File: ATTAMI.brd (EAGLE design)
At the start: 22.8 x 22.9 mm, 19 parts, among them J1 CON_HEADER_1X02-PTH, J2 MICRO-USB_ALIEXPRESS, J3 CON_HEADER_1X02-PTH, J4 CON_HEADER_1X06-PTH, U1 MIC5225, U2 ATTINY85

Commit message: ver 15b05
now the polygon back silkscreen logo placed correctly, ready for panalizing(!)
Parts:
- moved D4 0.37 mm to (20.5, 16.5)

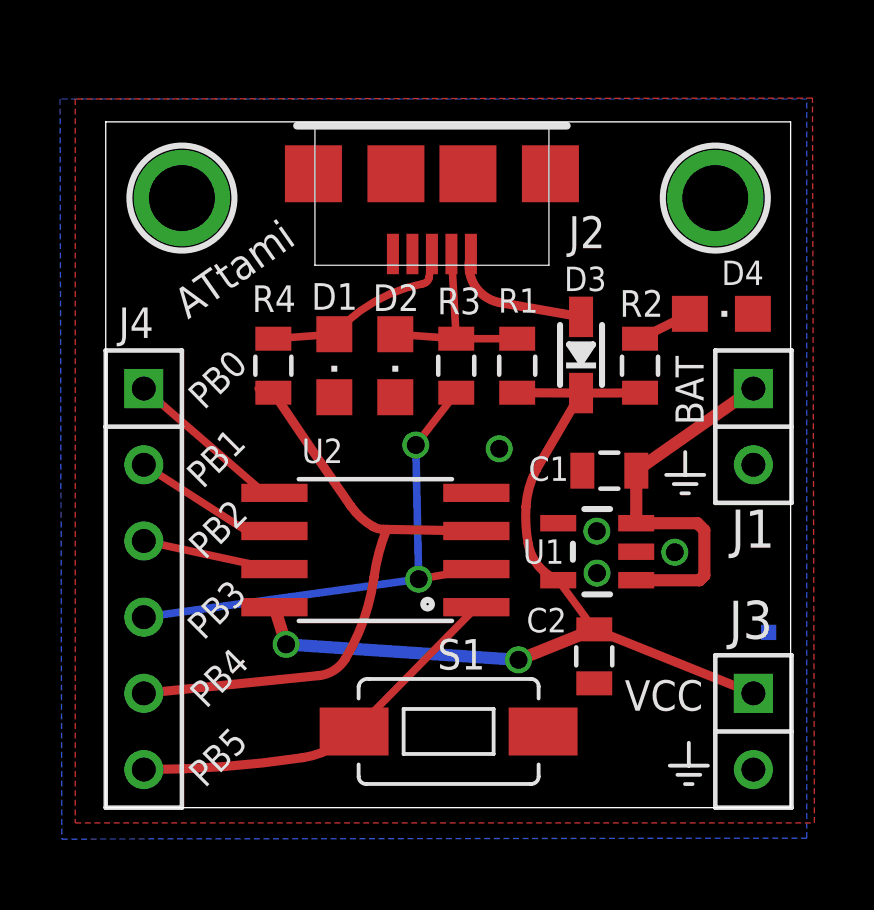
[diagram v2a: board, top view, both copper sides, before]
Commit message: 15b06
because of sobbing of online gerber checker 
https://www.freedfm.com/freedfm/0022376203858107/results/summary2.htm
- enlarge fonts on silkscreen to min 5mil 
- removed some redundant polygons from bottom silk
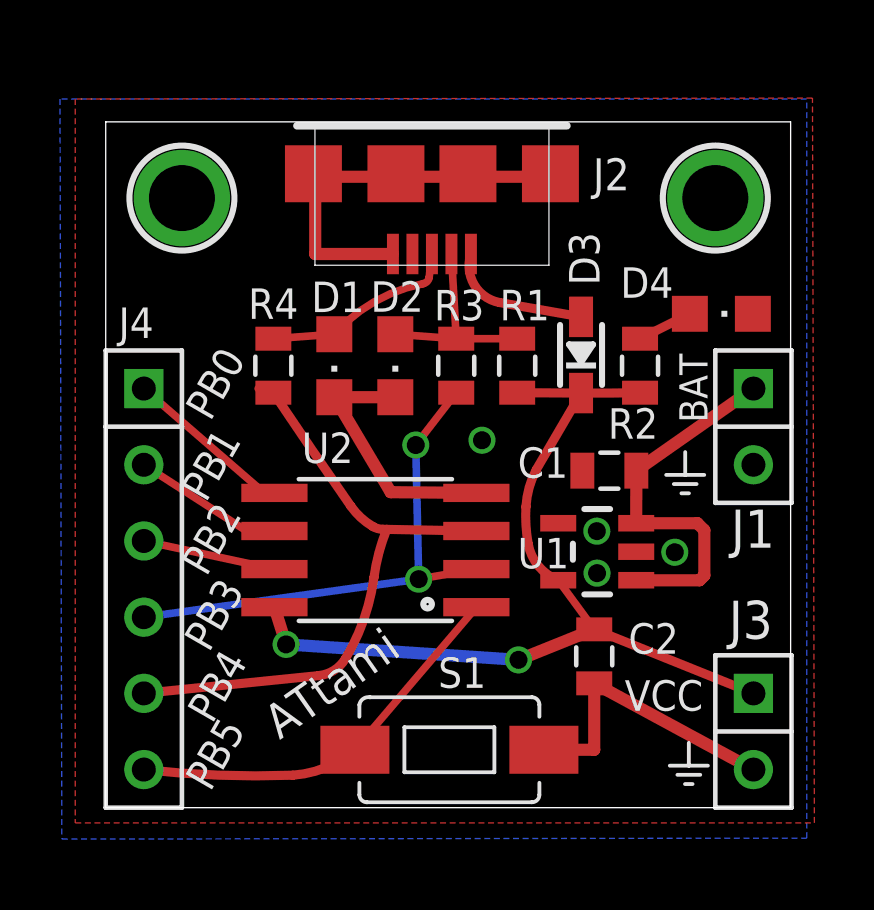
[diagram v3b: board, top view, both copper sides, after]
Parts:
- moved S1 0.61 mm to (11.5, 1.93)
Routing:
- net GND: track 0.00 -> 31.6 mm

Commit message: ver 17
changed the USB connector to the "official" package
MOLEX - 47346-0001 - MICRO USB TYPE B
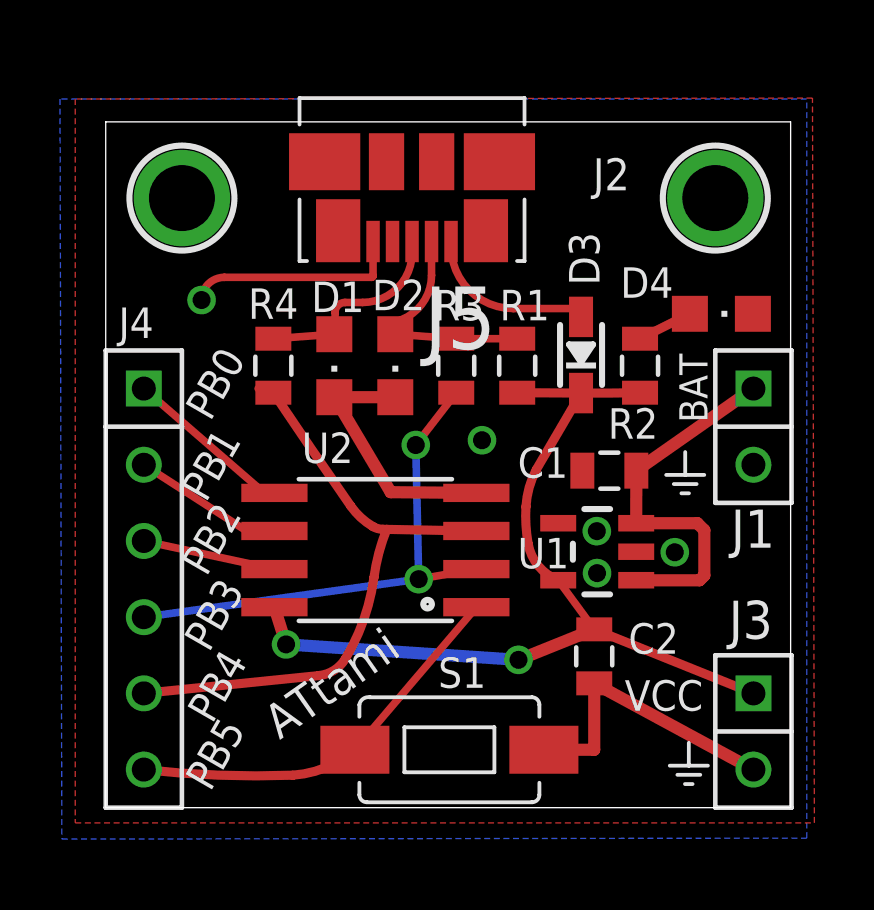
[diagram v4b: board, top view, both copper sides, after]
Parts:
- removed J2: MICRO-USB_ALIEXPRESS, yair_r:USB-MICRO-ALIEXPRESS
- added J5: (no value), Molex-47346-0001:MOLEX_47346-0001
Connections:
- removed net N$10: D2.A, J2.DM, R1.2, R3.1
- removed net N$7: D1.A, J2.DP, R4.1
- new net DM: D2.A, J5.2, R1.2, R3.1
- new net DP: D1.A, J5.3, R4.1
- net GND: now also J5.5; no longer J2.GND@1, J2.GND@2, J2.GND@3
- net V-BUS: now also J5.1; no longer J2.VCC
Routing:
- net DM: track 0.00 -> 7.98 mm
- net N$10: track 6.90 -> 0.00 mm
- net DP: track 0.00 -> 6.54 mm
- net N$7: track 6.52 -> 0.00 mm
- net GND: track 31.6 -> 25.7 mm, vias 4 -> 5
- net V-BUS: track 4.64 -> 5.47 mm

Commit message: sent to FAB
geekcon edition, with coincell
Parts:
- removed J4: CON_HEADER_1X06-PTH, dp_devices:M1X6
- removed J5: (no value), Molex-47346-0001:MOLEX_47346-0001
- added COIN_CELL, COIN_CELL_GND: (no value), adafruit:1X01-CLEANBIG
- added D5: Schottky, microbuilder:SOD-323
- added J2: (no value), microbuilder:1X02_ROUND
- added SJ1: (no value), microbuilder:SOLDERJUMPER_CLOSEDWIRE
- added USB: MICRO-USB_ALIEXPRESS, yair_r:USB-MICRO-ALIEXPRESS
- J1: value CON_HEADER_1X02-PTH -> (none); device dp_devices:M1X2 -> microbuilder:1X07_ROUND
- J3: value CON_HEADER_1X02-PTH -> (none); device dp_devices:M1X2 -> microbuilder:1X02_ROUND
- R2: value 560R -> 1K5
- moved J1 20.7 mm to (1.27, 8.89)
- moved C2 9.84 mm to (6.45, 5.37), turned to 0 degrees
- moved R2 1.22 mm to (18.2, 13.6)
- moved U2 0.65 mm to (8.85, 9.22)
- moved D3 0.42 mm to (16.1, 15.4)
- moved S1 0.28 mm to (11.2, 1.80)
- moved D4 0.25 mm to (20.8, 16.5), turned to 90 degrees
- moved D2 0.15 mm to (9.65, 14.6)
- moved D1 0.13 mm to (7.65, 14.6)
- moved C1 0.12 mm to (16.8, 11.1)
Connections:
- removed net DM: D2.A, J5.2, R1.2, R3.1
- removed net DP: D1.A, J5.3, R4.1
- new net N$10: D2.A, R1.2, R3.1, USB.DM
- new net N$13: D4.C, SJ1.2
- new net N$4: COIN_CELL.1, D5.AQ
- new net N$7: D1.A, R4.1, USB.DP
- net GND: now also COIN_CELL_GND.1, J1.1, J2.2, SJ1.1, USB.GND@1, USB.GND@2, USB.GND@3, USB.P$10, USB.P$9; no longer D4.C, J1.2, J5.5
- net N$1: now also J1.5; no longer J4.4
- net N$15: now also J1.3; no longer J4.2
- net N$3: now also J1.2; no longer J4.1
- net N$5: now also J1.4; no longer J4.3
- net N$6: now also J1.6; no longer J4.5
- net N$8: now also J1.7; no longer J4.6
- net V-BUS: now also D3.AQ, USB.VCC; no longer D3.A, J5.1
- net VCC: now also D3.CQ, D5.CQ; no longer D3.C
- net V_BAT: now also J2.1; no longer J1.1
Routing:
- net GND: track 25.7 -> 8.52 mm, vias 5 -> 4
- net DM: track 7.98 -> 0.00 mm
- net N$10: track 0.00 -> 6.97 mm
- net VCC: track 30.7 -> 37.5 mm
- net N$7: track 0.00 -> 6.72 mm
- net DP: track 6.54 -> 0.00 mm
- net V_BAT: track 12.8 -> 6.82 mm
- net N$13: track 0.00 -> 3.34 mm, vias 0 -> 1
- net N$4: track 0.00 -> 2.77 mm
- net N$11: track 1.86 -> 4.18 mm
- net N$6: track 21.0 -> 22.8 mm
- net N$8: track 13.4 -> 15.0 mm
- net N$1: track 17.9 -> 16.7 mm

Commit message: fix floating pin
major error in voltage regualtor (U1).  enable pin was not connected to
VBAT in GKx  batch :(.
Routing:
- net V_BAT: track 6.82 -> 11.2 mm
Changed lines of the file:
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@@
 <wire x1="17.69538125" y1="11.109059375" x2="18.729059375" y2="11.109059375" width="0.4064" layer="1"/>
 <wire x1="18.729059375" y1="11.109059375" x2="21.59" y2="13.97" width="0.4064" layer="1"/>
-<wire x1="17.78" y1="7.62" x2="17.683103125" y2="9.4818625" width="0" layer="19" extent="1-1"/>
+<wire x1="17.683103125" y1="9.4818625" x2="18.923" y2="9.4818625" width="0.4064" layer="1"/>
+<wire x1="18.923" y1="9.4818625" x2="18.923" y2="7.62" width="0.4064" layer="1"/>
+<wire x1="18.923" y1="7.62" x2="17.683103125" y2="7.62" width="0.4064" layer="1"/>
+<wire x1="17.683103125" y1="7.62" x2="17.683103125" y2="7.5818625" width="0.4064" layer="1"/>
 </signal>
 <signal name="N$7">

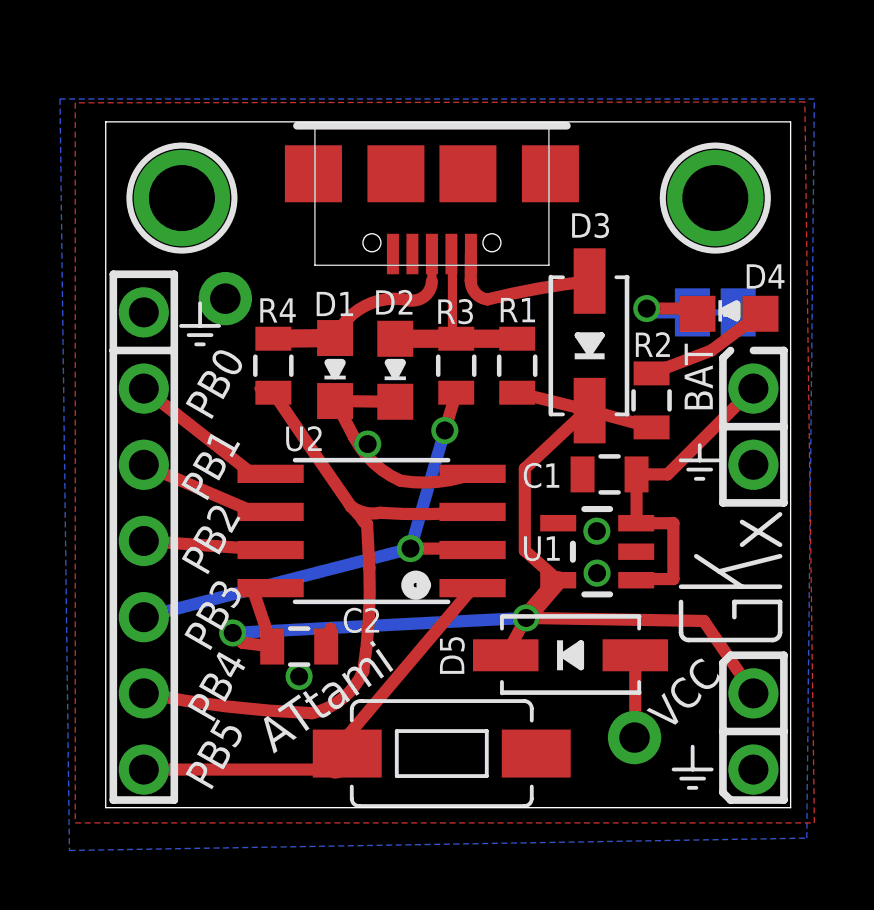
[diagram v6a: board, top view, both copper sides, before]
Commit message: expanded microusb pads
also add OSHW logo
and removed some drawings
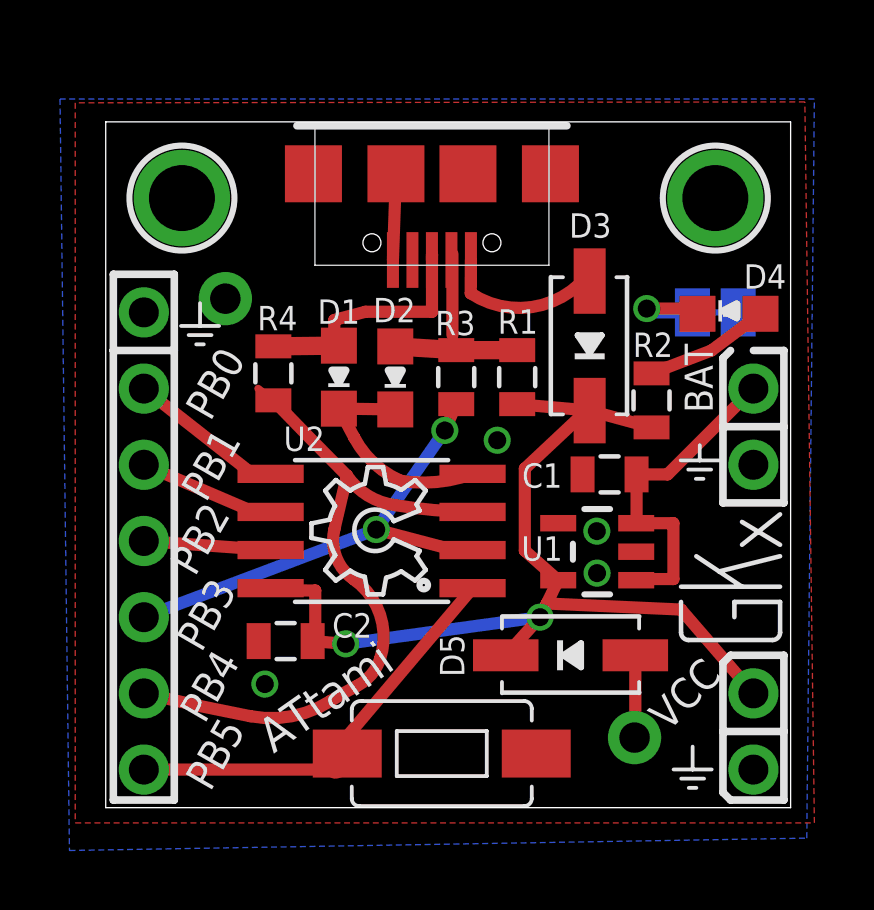
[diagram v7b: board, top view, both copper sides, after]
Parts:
- added U$3: (no value), ohw-logo:OSHW_6X150_NOTEXT
- moved C2 0.49 mm to (6.00, 5.55), turned to 180 degrees
- moved R1 0.38 mm to (13.7, 14.4)
- moved R3 0.38 mm to (11.7, 14.4)
- moved D1 0.28 mm to (7.77, 14.4)
- moved D2 0.25 mm to (9.65, 14.3)
- moved R4 0.25 mm to (5.59, 14.5)
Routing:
- net VCC: track 37.5 -> 35.2 mm
- net GND: track 8.52 -> 10.4 mm
- net N$7: track 6.72 -> 8.52 mm
- net N$6: track 22.8 -> 23.6 mm
- net N$10: track 6.97 -> 7.49 mm
